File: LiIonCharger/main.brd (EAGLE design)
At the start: 8 parts, among them IC1 MCP73831

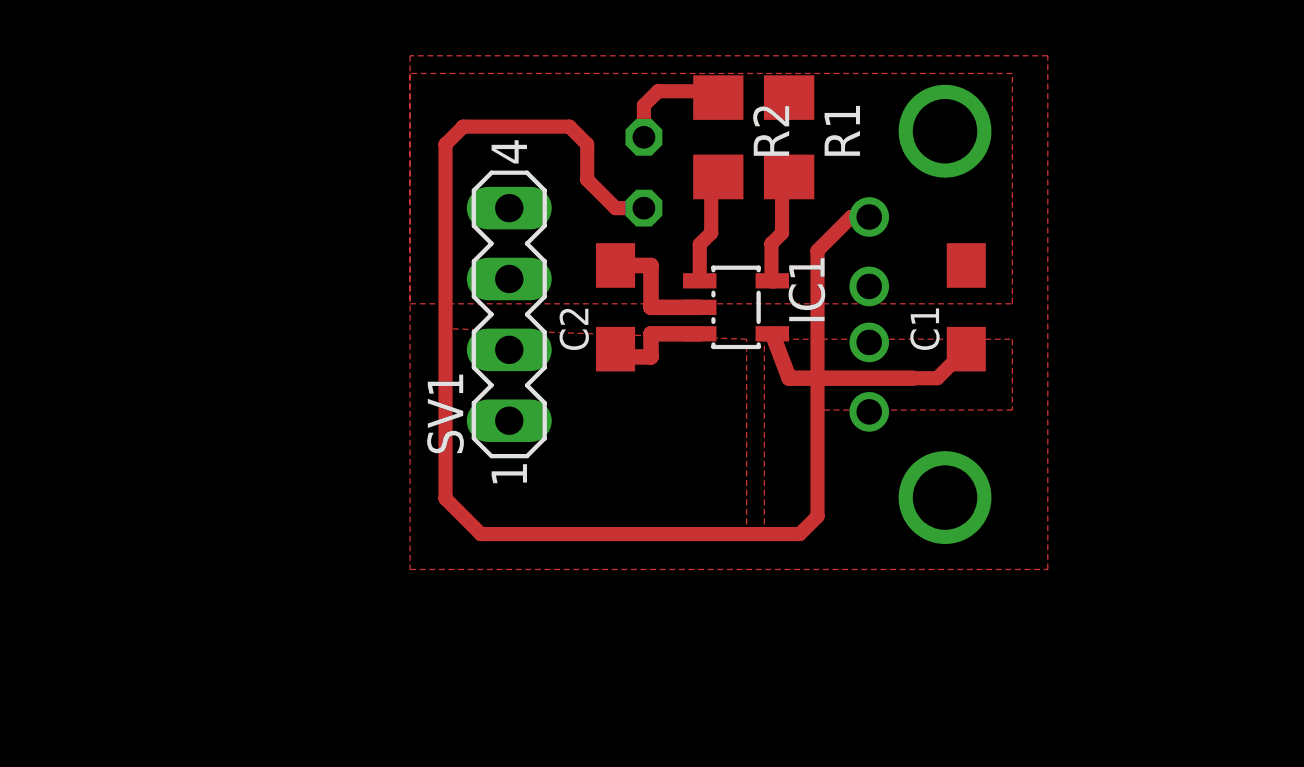
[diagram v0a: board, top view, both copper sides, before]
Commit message: Fixed to be only on one layer.
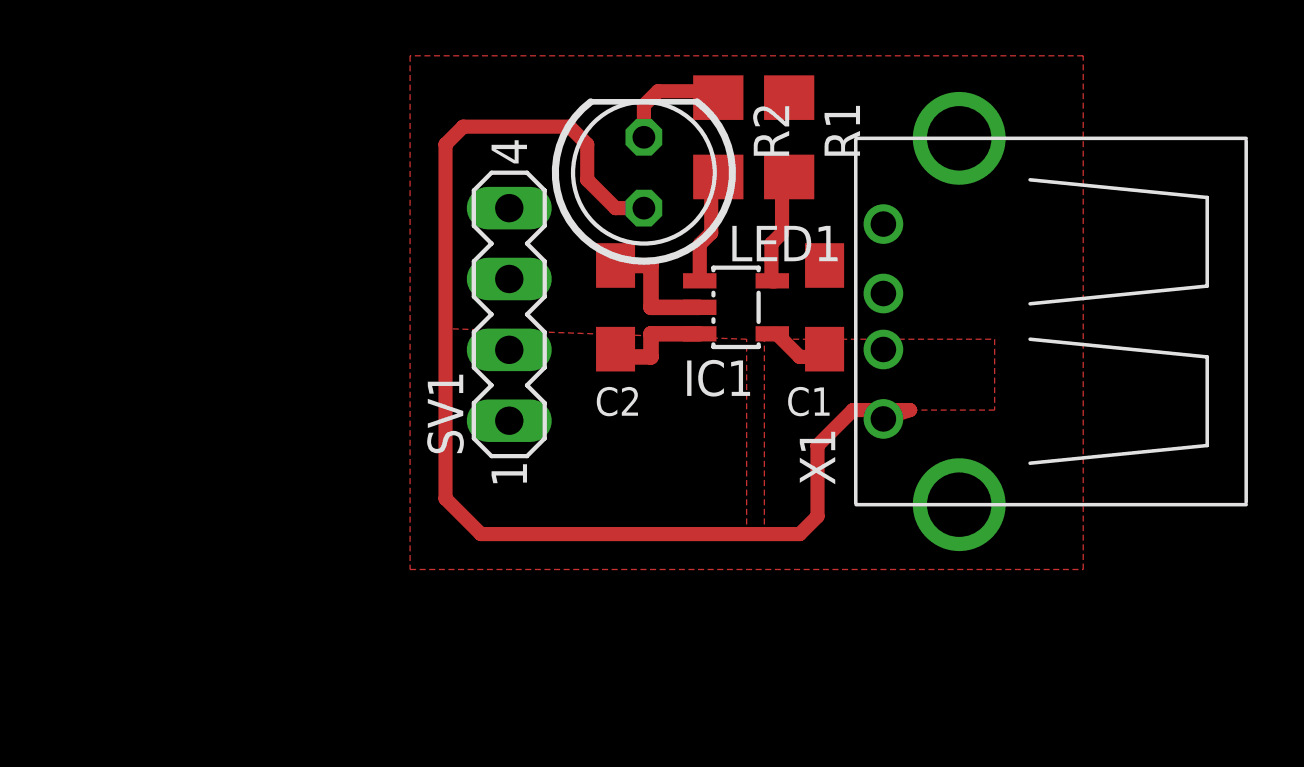
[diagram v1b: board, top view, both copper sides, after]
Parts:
- moved C1 5.08 mm to (27.6, 14.5)
- moved X1 0.57 mm to (32.4, 14.0), flipped to the top, turned to 180 degrees
- flipped LED1 to the top
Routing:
- net VCC: track 56.5 -> 45.9 mm

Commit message: 7 Segment LED Display project added.
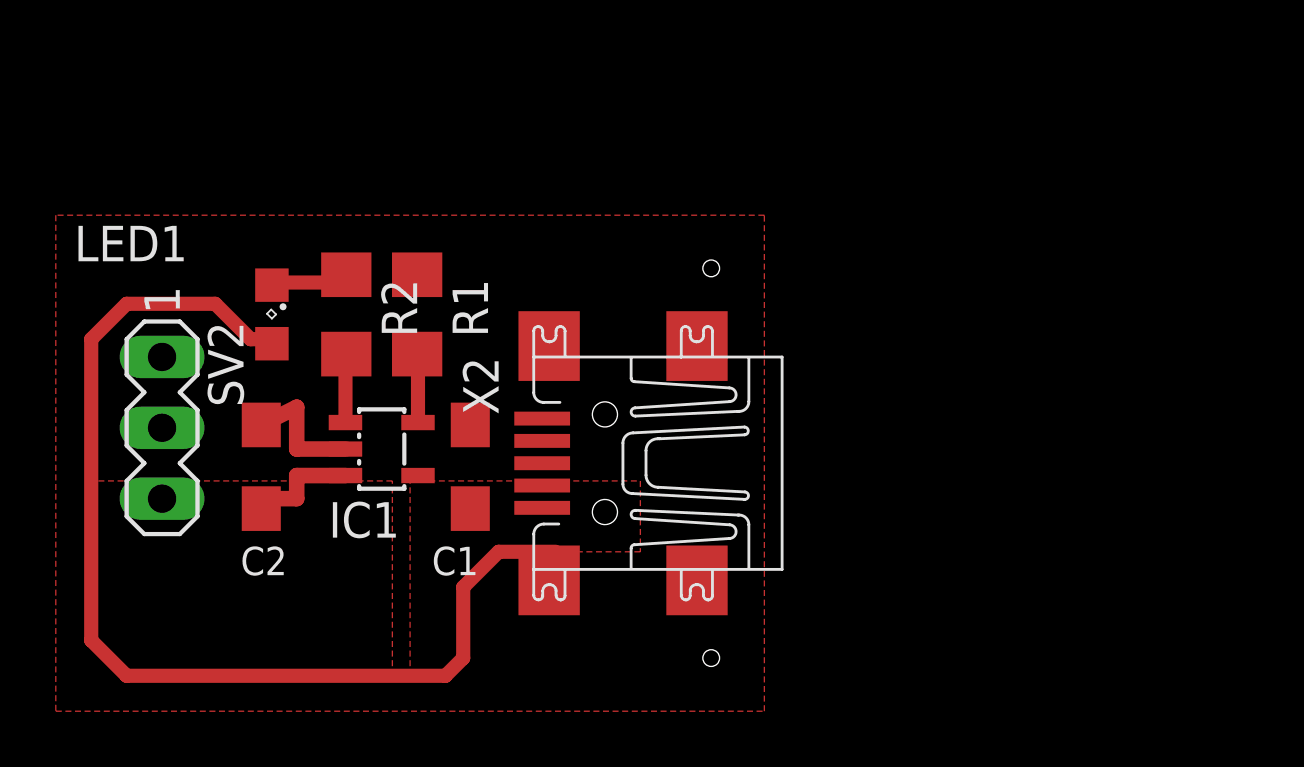
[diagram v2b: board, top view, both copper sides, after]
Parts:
- removed SV1: (no value), con-lstb:MA04-1
- removed X1: (no value), con-usb-3:USB-A-H
- added SV2: (no value), con-lstb:MA03-1
- added X2: MINI-USB-UX60-MB-5ST, con-hirose:UX60-MB-5ST
- LED1: device led:LED5MM -> led:SML0805
- moved R1 14.8 mm to (13.0, 14.2)
- moved R2 14.8 mm to (10.4, 14.2)
- moved LED1 14.3 mm to (7.75, 14.2), turned to 270 degrees
- moved C1 13.9 mm to (14.9, 8.76)
- moved C2 13.9 mm to (7.37, 8.76)
- moved IC1 13.7 mm to (11.7, 9.40)
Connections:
- net GND: now also SV2.2, X2.5; no longer SV1.3, X1.GND
- net N$2: now also LED1.C; no longer LED1.K
- net N$4: now also SV2.3; no longer SV1.1
- net VCC: now also X2.1; no longer X1.VBUS
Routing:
- net VCC: track 45.9 -> 39.5 mm
- net N$1: track 4.16 -> 2.47 mm
- net N$3: track 4.00 -> 2.47 mm
- net N$2: track 4.12 -> 3.11 mm
